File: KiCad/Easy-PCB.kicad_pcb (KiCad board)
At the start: 2 copper layers, 97 parts, among them J1 703W-00/53, J3 HLW20R-2C7LF, K1 G5LE-1A-E_DC12, P1 1x02, P12 M20-9980346, P2 1x06, P24 M20-9980346, P3 1x04, P4 1x03, P5 1x02, Q1 2N3904, Q10 MJE350, Q11 2N3904, Q12 2N3904, Q13 MJE340, Q14 MJE350, Q15 2N3904, Q16 MJE340, Q17 MJE350, Q18 2N3904, Q19 2N3904, Q2 MJE340, Q3 2N3904, Q4 2N3904, Q5 MJE340, Q6 MJE350, Q7 2N3904, Q8 2N3904, Q9 MJE340, SW1 R1966ABLKBLKFR, T1 VPP24-830, U1 PIC16F883, U2 MCP41050, U3 MCP617, U4 MCP9700A, U5 LM7805

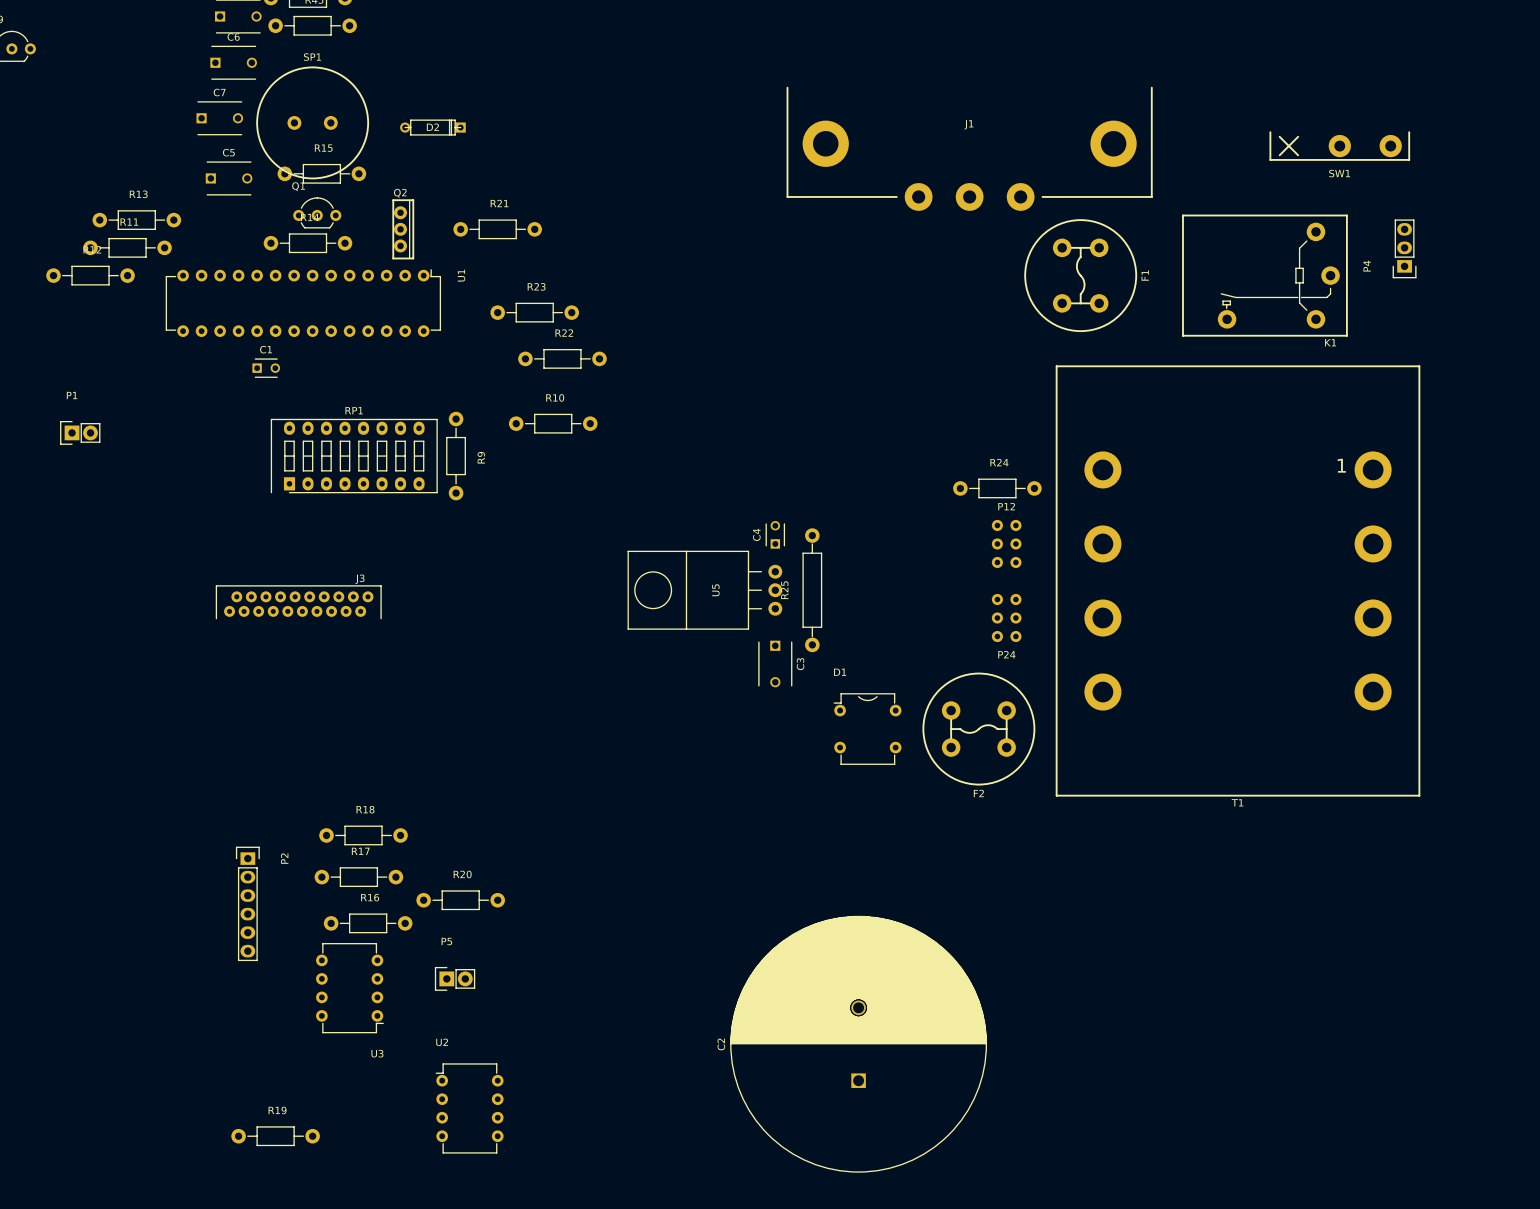
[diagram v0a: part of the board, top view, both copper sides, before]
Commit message: power port, switch, transformer, and relay in place
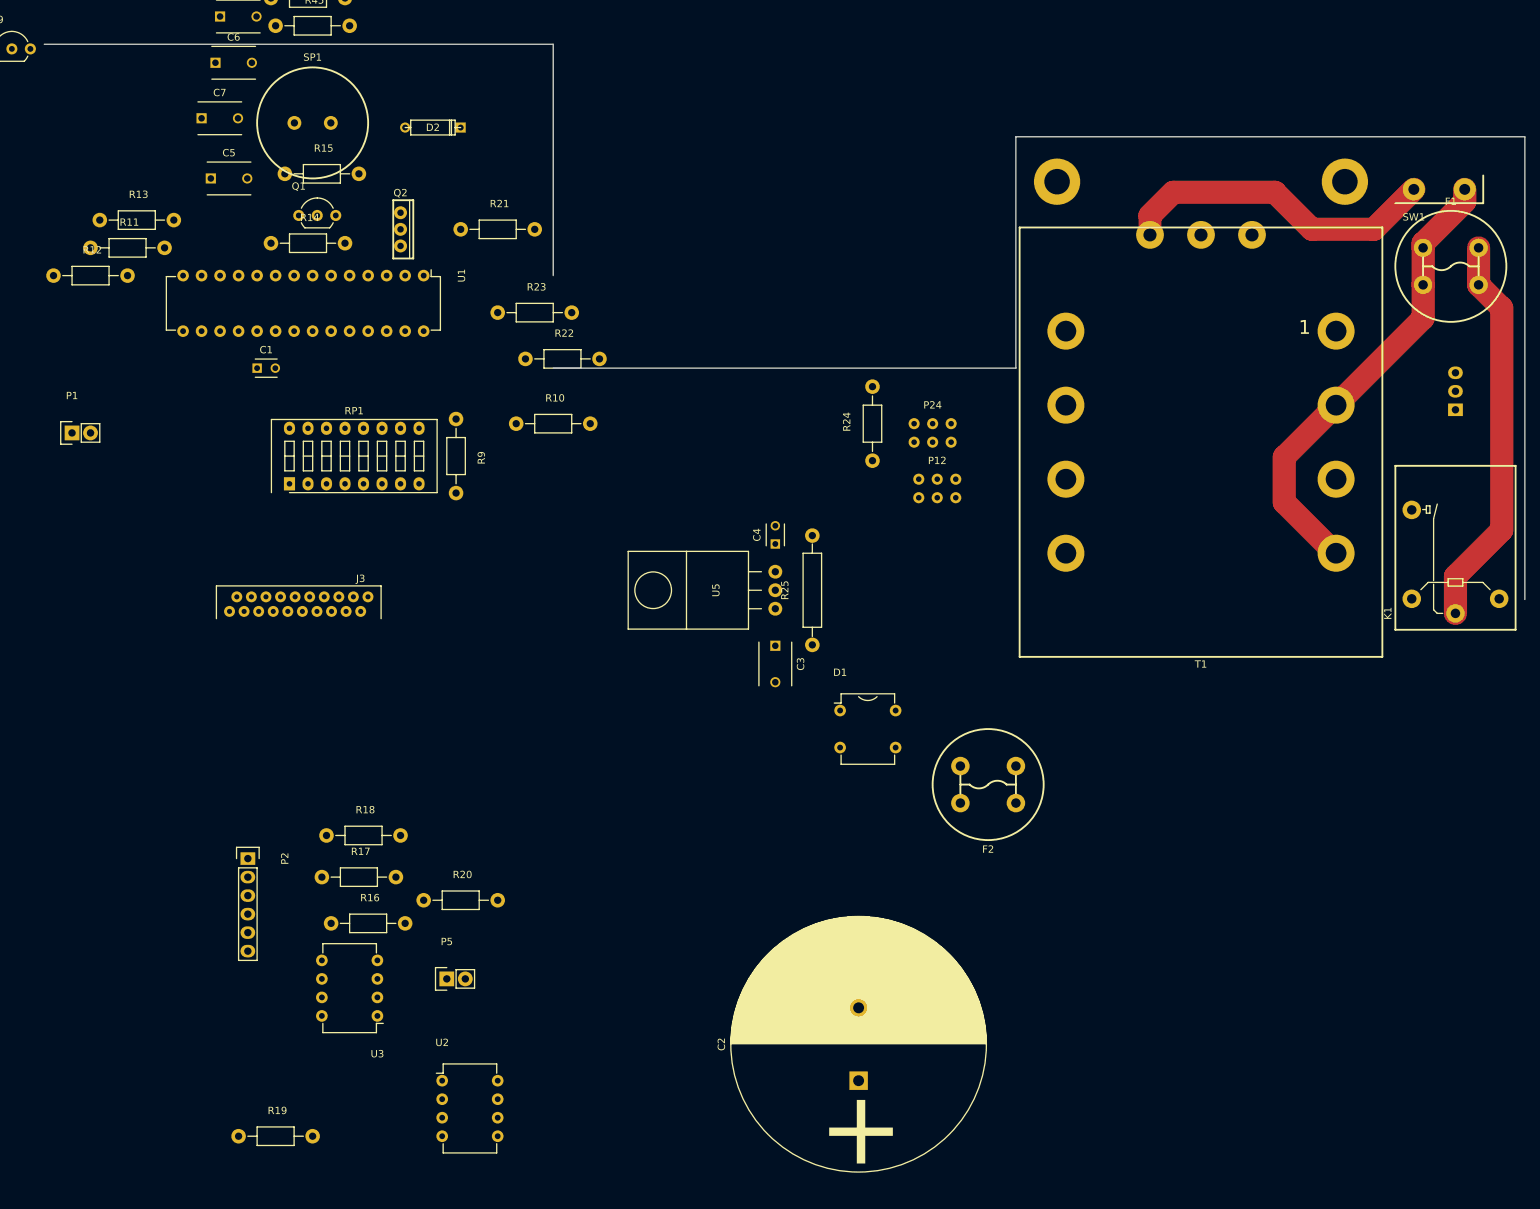
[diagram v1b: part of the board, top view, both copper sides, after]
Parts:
- C1, C4: footprint Capacitors_ThroughHole:C_Disc_D3_P2.5 -> Easy-PCB-footprints:C_Disc_D3_P2.5
- C2: footprint Capacitors_ThroughHole:C_Radial_D35_L51_P10 -> Easy-PCB-footprints:C_Radial_D35_L51_P10
- C3, C5, C6, C7, C8: footprint Capacitors_ThroughHole:C_Disc_D6_P5 -> Easy-PCB-footprints:C_Disc_D6_P5
- J1, P4: moved to B.Cu
- U5: footprint TO-220 -> Easy-PCB-footprints:TO-220
- moved F1 50.8 mm to (218.4, 55.9), turned to 0 degrees
- moved K1 49.4 mm to (219.1, 103.5), turned to 90 degrees
- moved J1 33.5 mm to (184.2, 35.6), turned to 180 degrees
- moved P24 27.4 mm to (147.3, 78.7), turned to 270 degrees
- moved P4 20.9 mm to (219.1, 75.6)
- moved T1 19.7 mm to (184.2, 80.0)
- moved R24 19.3 mm to (139.1, 77.5), turned to 90 degrees
- moved SW1 14.4 mm to (213.4, 29.2)
- moved P12 12.2 mm to (148.0, 86.4), turned to 90 degrees
- moved F2 7.73 mm to (154.9, 127.0)
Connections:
- K1 pad 1: /Heat Relay/HeatLive -> VAA
- K1 pad 3: VAA -> /Heat Relay/HeatLive
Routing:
- net /Power Circuit/MainsLive: track 0.00 -> 63.2 mm
- net VAA: track 0.00 -> 54.1 mm
- net Net-(J1-Pad1): track 0.00 -> 44.6 mm
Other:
- board outline added: 203.2 x 76.2 mm
- net class Vac added: clearance 1.4478, trace_width 3.175, via_dia 0.6, via_drill 0.4

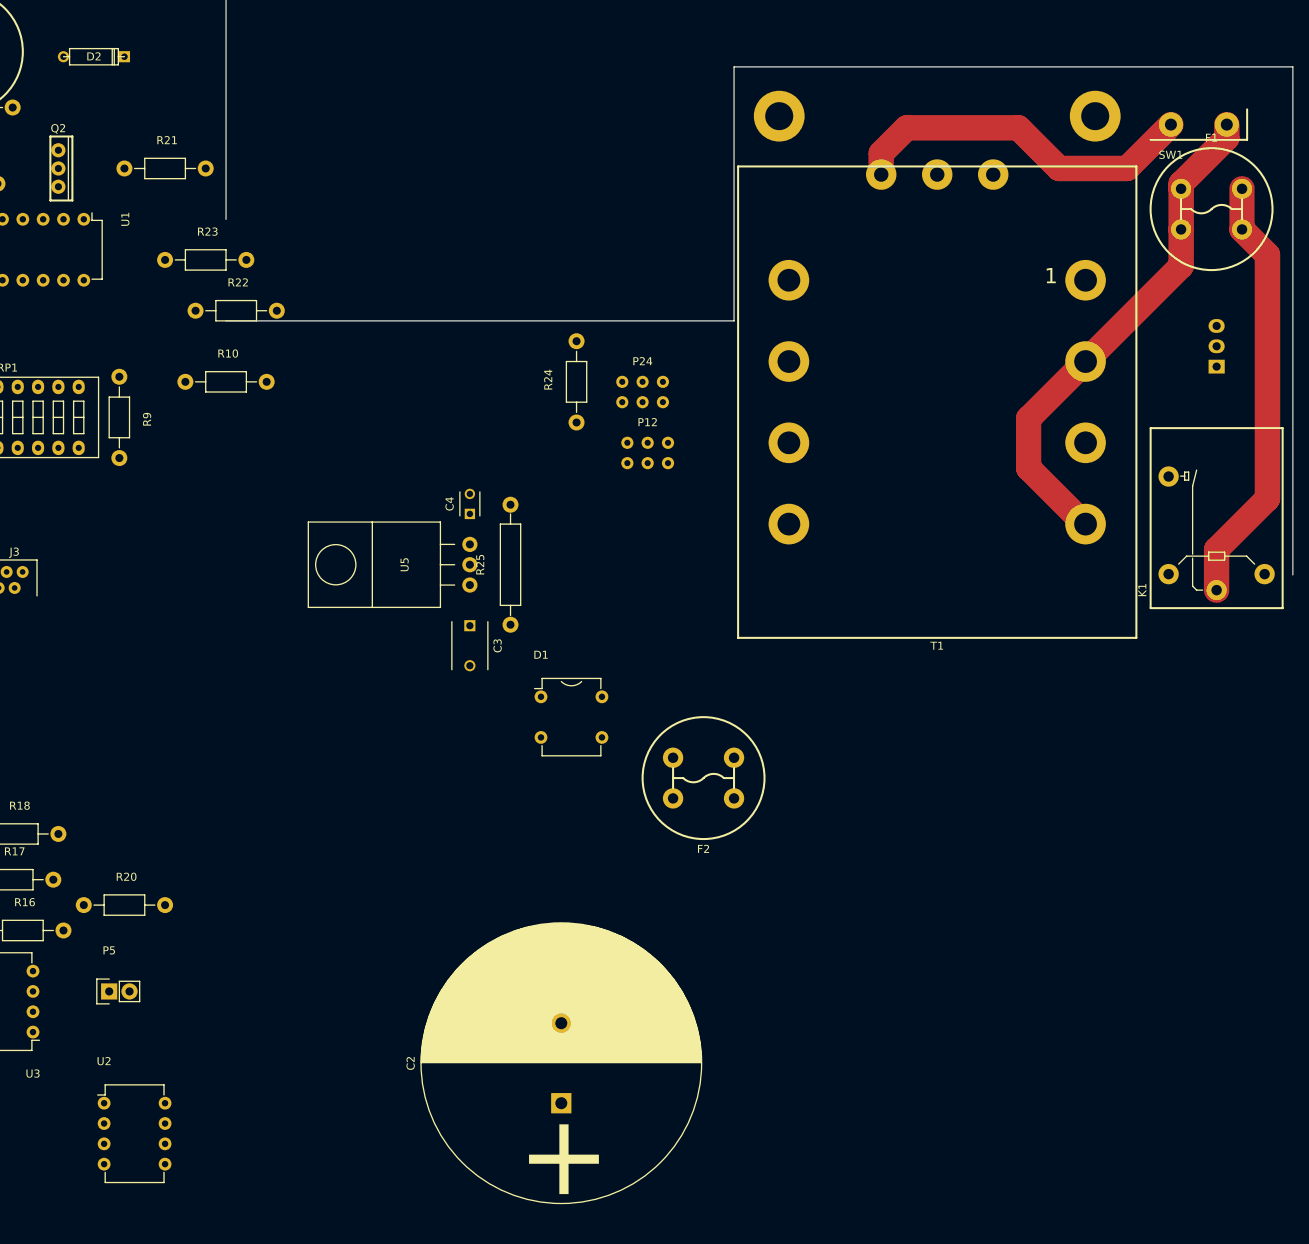
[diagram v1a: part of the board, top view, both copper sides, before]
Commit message: power supply placed and routed
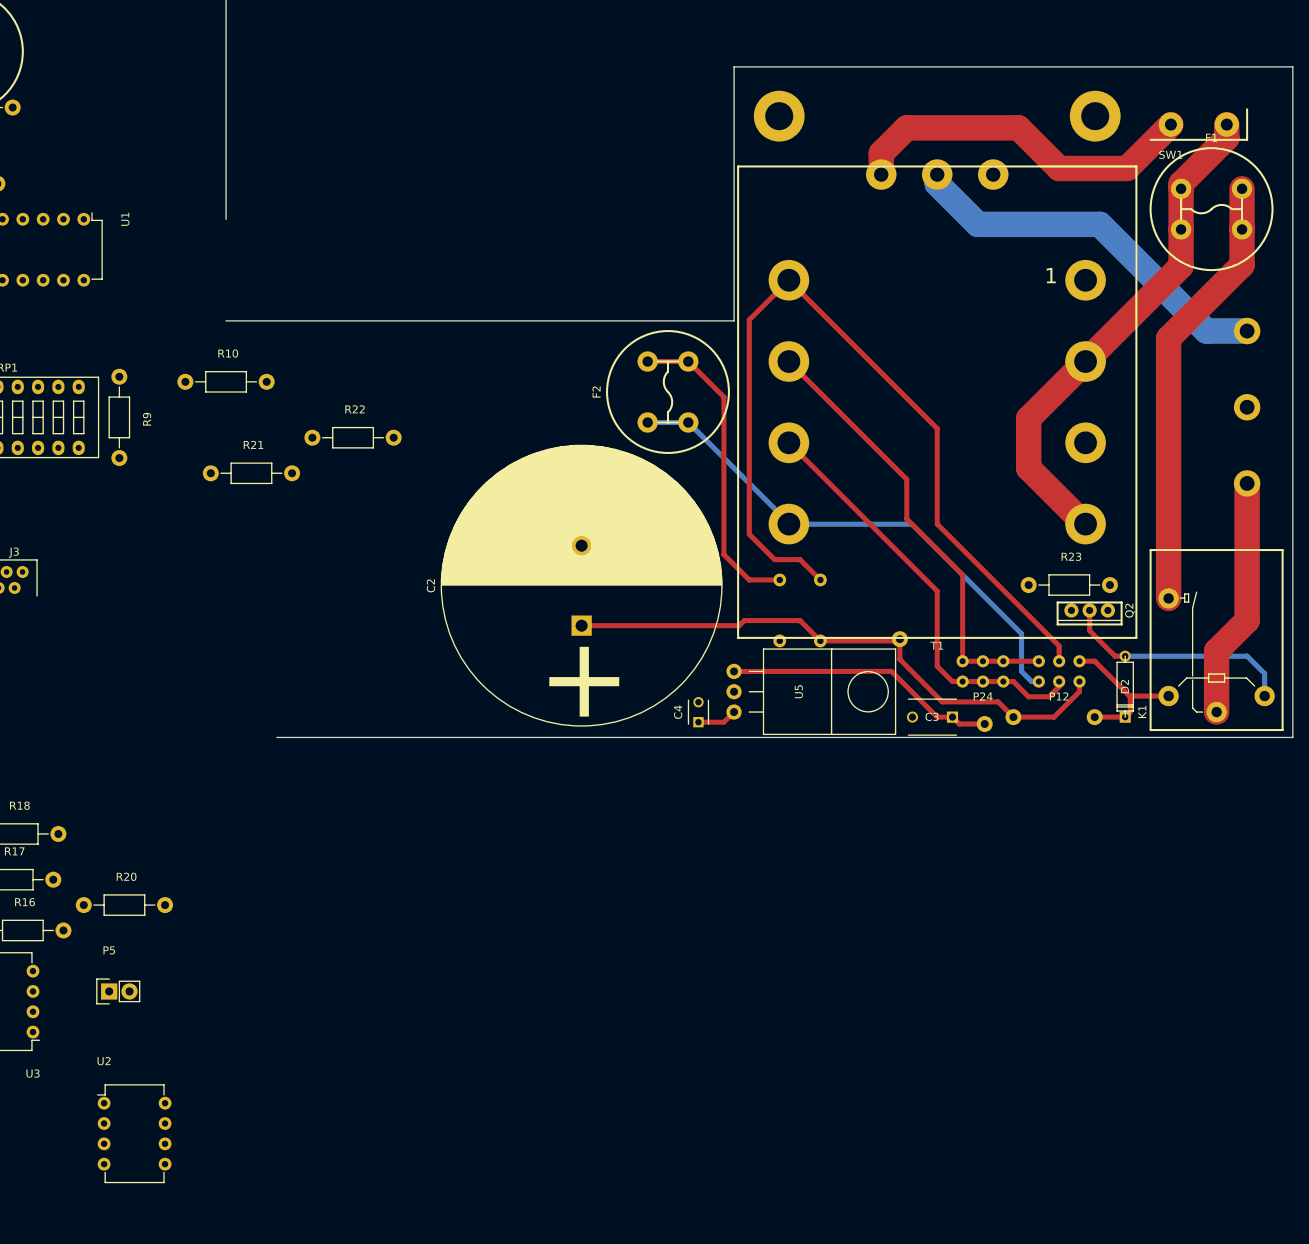
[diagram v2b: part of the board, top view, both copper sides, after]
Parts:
- D1, R24, R25: moved to B.Cu
- P12: moved to F.Cu
- P4: value 1x03 -> 1x03 Terminal Block; footprint Socket_Strips:Socket_Strip_Straight_1x03 -> Easy-PCB-footprints:5-1437652-4
- moved D2 151.1 mm to (207.6, 115.6), turned to 270 degrees
- moved Q2 140.2 mm to (203.2, 106.0), turned to 270 degrees
- moved R23 115.3 mm to (200.7, 102.9)
- moved R24 72.9 mm to (198.8, 119.4), turned to 0 degrees
- moved C3 61.4 mm to (186.1, 119.4), turned to 180 degrees
- moved C2 59.7 mm to (139.7, 108.0)
- moved P12 58.2 mm to (199.4, 113.7)
- moved R25 55.9 mm to (184.8, 114.9), turned to 135 degrees
- moved P24 55.0 mm to (189.9, 113.7), turned to 90 degrees
- moved F2 48.5 mm to (150.5, 78.7), turned to 90 degrees
- moved R21 39.6 mm to (98.4, 88.9)
- moved C4 38.7 mm to (154.3, 120.0)
- moved U5 36.6 mm to (158.8, 116.2), turned to 270 degrees
- moved D1 35.6 mm to (169.5, 109.9), turned to 90 degrees
- moved R22 21.6 mm to (111.1, 84.5)
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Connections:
- net Net-(C3-Pad1) renamed VDDunreg
- net Net-(D1-Pad3) renamed 12or24VAC5
- net Net-(D2-Pad2) renamed 12Vrelay2
- D1 pad 4: Net-(D1-Pad4) -> 12or24VAC2
- D2 pad 1: +12V -> 12Vrelay1
- F2 pad 1: Net-(F2-Pad1) -> 12or24VAC1
- F2 pad 2: Net-(F2-Pad1) -> 12or24VAC1
- K1 pad 1: VAA -> /Heat Relay/HeatLive
- K1 pad 2: +12V -> 12Vrelay1
- K1 pad 3: /Heat Relay/HeatLive -> VAA
- P12 pad 1: +12V -> 12or24VAC1
- P12 pad 2: VCC -> 12or24VAC4
- P12 pad 3: Net-(D1-Pad4) -> 12or24VAC3
- P12 pad 4: Net-(P12-Pad4) -> 12or24VAC2
- P12 pad 5: Net-(P12-Pad5) -> VCC
- P12 pad 6: Net-(F2-Pad1) -> 12Vrelay1
- P24 pad 1: Net-(P12-Pad4) -> 12or24VAC3
- P24 pad 2: Net-(P12-Pad5) -> 12or24VAC4
- P24 pad 3: Net-(P12-Pad4) -> 12or24VAC3
- P24 pad 4: Net-(P12-Pad5) -> 12or24VAC4
- P24 pad 5: Net-(P12-Pad4) -> 12or24VAC3
- P24 pad 6: Net-(P12-Pad5) -> 12or24VAC4
- R24 pad 2: +12V -> 12Vrelay1
- T1 pad 10: Net-(P12-Pad4) -> 12or24VAC3
- T1 pad 12: Net-(F2-Pad1) -> 12or24VAC1
- T1 pad 7: Net-(D1-Pad4) -> 12or24VAC2
- T1 pad 9: Net-(P12-Pad5) -> 12or24VAC4
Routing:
- net 12or24VAC2: track 0.00 -> 108.7 mm
- net VCC: track 0.00 -> 71.7 mm
- net 12or24VAC1: track 0.00 -> 65.1 mm
- net 12or24VAC4: track 0.00 -> 56.0 mm
- net 12or24VAC3: track 0.00 -> 53.6 mm
- net Earth: track 0.00 -> 47.5 mm
- net 12or24VAC5: track 0.00 -> 39.4 mm
- net VDDunreg: track 0.00 -> 34.1 mm
- net /Heat Relay/HeatLive: track 0.00 -> 30.2 mm
- net 12Vrelay2: track 0.00 -> 29.4 mm
- net 12Vrelay1: track 0.00 -> 19.7 mm
- net VDD: track 0.00 -> 4.97 mm
- net VAA: track 54.1 -> 55.0 mm
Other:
- board size 203.2 x 76.2 mm -> 203.2 x 96.5 mm
- net class Vcc added: clearance 0.762, trace_width 0.635, via_dia 0.6, via_drill 0.4
- net class Vdd added: clearance 0.508, trace_width 0.635, via_dia 0.6, via_drill 0.4
